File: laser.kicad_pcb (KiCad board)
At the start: 4 copper layers, 90.2 x 50.9 mm, 124 parts, among them IC201 ADM7172ACPZ-4.2-R7, IC202 LT1716CS5#TRPBF, IC203 ADM7154ARDZ-3.3-R7, IC204 IRF9358PBF, IC601 ATMEGA328P-AU, IC602 FT232RL-TUBE, IC701 MAX6126AASA25+, IC801 ADS122C04IPWR, J601 M20-9980345, J602 USB_Connector, Q401 RSR030N06TL, U101 281698-3, U201 LM4040EIM3X-2.5_NOPB, U301 OPA569AIDWPR, U302 OPA569AIDWPR, U401 ADA4528-2ACPZ-RL, U402 782853152_WE-CBA_08, U501 ADA4528-2ACPZ-RL, U502 ADA4528-2ACPZ-RL, U801 MAX5217GUA+, U802 MAX5217GUA+, Y601 ECS-160-16-33B-CKM-TR

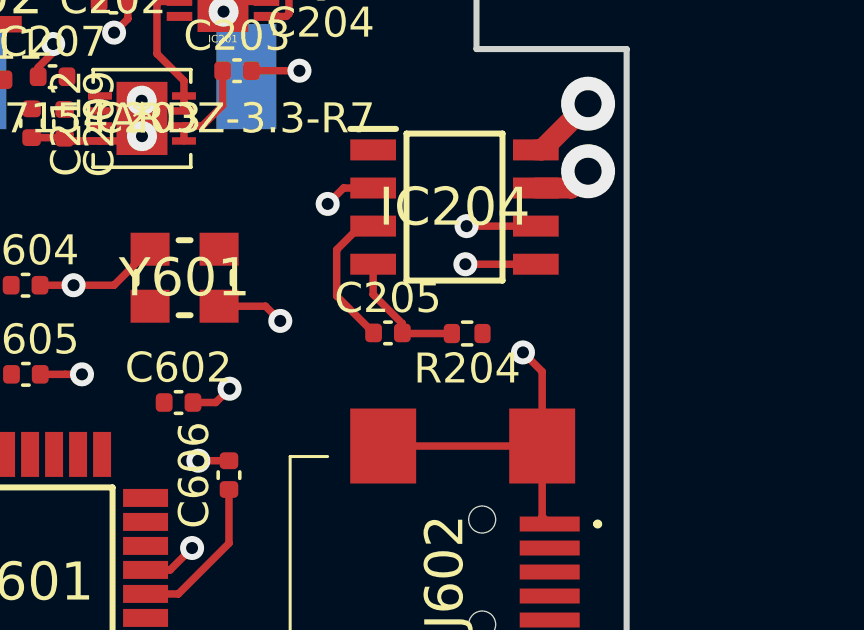
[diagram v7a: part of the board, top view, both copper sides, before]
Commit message: added more traces, plus a few grounds. vias on epads as well
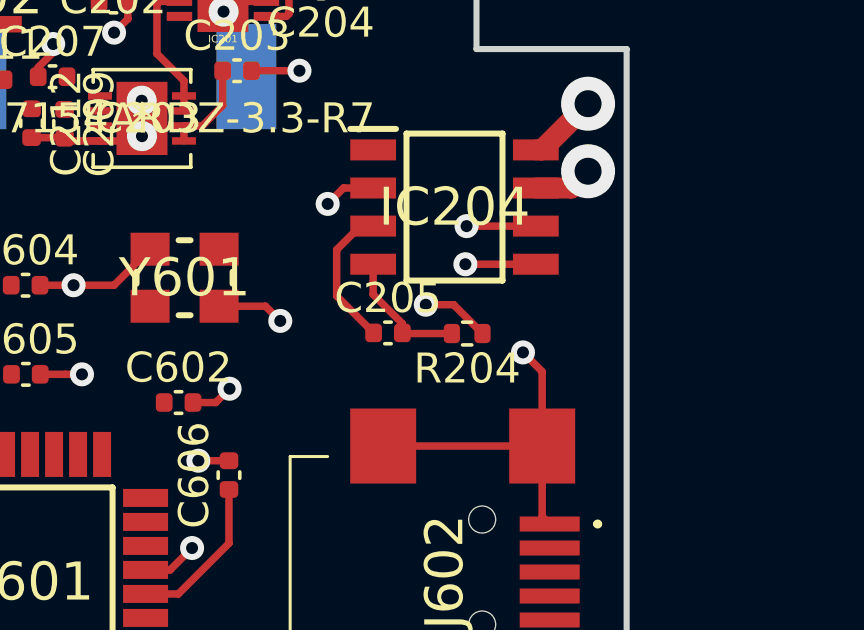
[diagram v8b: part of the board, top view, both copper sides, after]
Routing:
- net Net-(IC202-Pad1): track 0.00 -> 2.29 mm, vias 0 -> 1
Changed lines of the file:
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@@
     (thickness 1.6)
     (drawings 17)
-    (tracks 368)
+    (tracks 371)
     (zones 0)
     (modules 124)
@@
   (segment (start 207.61 94.5) (end 207.61 94.5) (width 0.25) (layer F.Cu) (net 16))
   (via (at 207.61 94.5) (size 0.8) (drill 0.4) (layers F.Cu B.Cu) (net 16))
+  (via (at 206.29 95.85) (size 0.8) (drill 0.4) (layers F.Cu B.Cu) (net 37))
   (segment (start 198.83 129.14) (end 198.83 130.43) (width 0.25) (layer F.Cu) (net 19))
   (segment (start 197.82 128.13) (end 198.83 129.14) (width 0.25) (layer F.Cu) (net 19))
@@
   (segment (start 192.83 128.74) (end 192.82 128.73) (width 0.25) (layer F.Cu) (net 35))
   (segment (start 192.83 130.64) (end 192.83 128.74) (width 0.25) (layer F.Cu) (net 35))
+  (segment (start 207.22 95.85) (end 206.29 95.85) (width 0.25) (layer F.Cu) (net 37))
+  (segment (start 208.18 96.81) (end 207.22 95.85) (width 0.25) (layer F.Cu) (net 37))
   (segment (start 187.744 89.094) (end 185.6 86.95) (width 0.25) (layer F.Cu) (net 39))
   (segment (start 187.744 89.199999) (end 187.744 89.094) (width 0.25) (layer F.Cu) (net 39))
